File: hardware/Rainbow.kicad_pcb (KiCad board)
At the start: 2 copper layers, 53.2 x 38.7 mm, 22 parts, among them J1 PICKit3, J2 UART, J3 JUMPER, J4 JACK, J5 RGB, J6 RGB, J7 RGB, J8 RGB, J9 SOURCE, Q1 Q_NMOS_GDS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

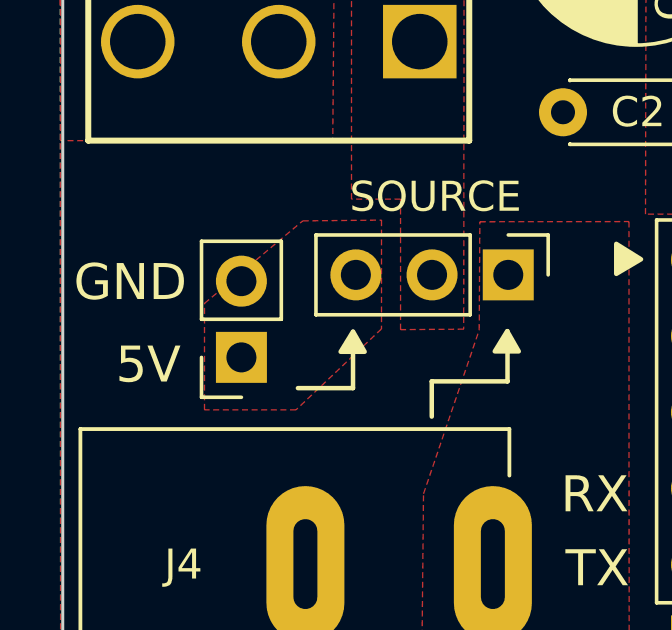
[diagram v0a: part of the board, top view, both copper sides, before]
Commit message: Folder renaming
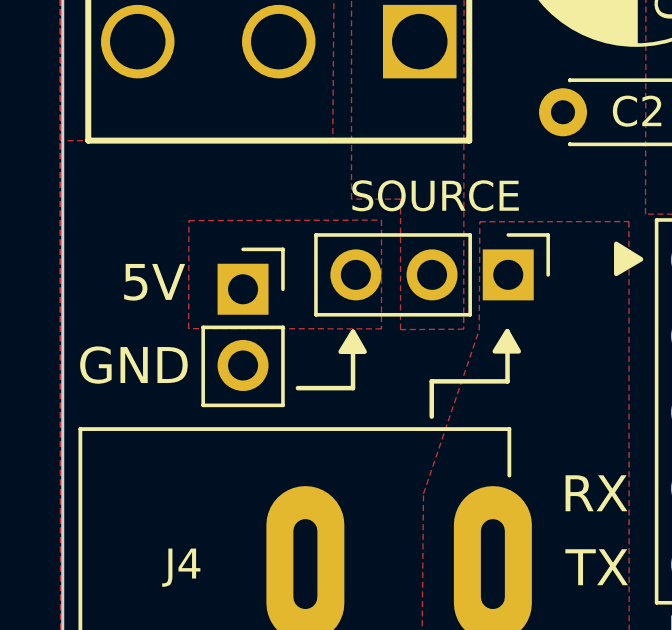
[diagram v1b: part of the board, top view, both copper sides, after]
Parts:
- moved J3 2.27 mm to (95.5, 77.4), turned to 0 degrees
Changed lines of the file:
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@@
   )
   (footprint "Connector_PinSocket_2.54mm:PinSocket_1x02_P2.54mm_Vertical" (layer "F.Cu")
-    (at 95.43 79.7 180)
+    (at 95.485 77.43)
     (descr "Through hole straight socket strip, 1x02, 2.54mm pitch, single row (from Kicad 4.0.7), script generated")
     (tags "Through hole socket strip THT 1x02 2.54mm single row")
@@
     (fp_line (start -1.27 -1.27) (end 0.635 -1.27) (layer "F.Fab") (width 0.1))
     (fp_line (start 0.635 -1.27) (end 1.27 -0.635) (layer "F.Fab") (width 0.1))
-    (pad "1" thru_hole rect (at 0 0 180) (size 1.7 1.7) (drill 1) (layers *.Cu *.Mask)
+    (pad "1" thru_hole rect (at 0 0) (size 1.7 1.7) (drill 1) (layers *.Cu *.Mask)
       (net 13 "Net-(J3-Pad1)") (pinfunction "Pin_1") (pintype "passive"))
-    (pad "2" thru_hole oval (at 0 2.54 180) (size 1.7 1.7) (drill 1) (layers *.Cu *.Mask)
+    (pad "2" thru_hole oval (at 0 2.54) (size 1.7 1.7) (drill 1) (layers *.Cu *.Mask)
       (net 1 "GNDREF") (pinfunction "Pin_2") (pintype "passive"))
     (model "${KICAD6_3DMODEL_DIR}/Connector_PinSocket_2.54mm.3dshapes/PinSocket_1x02_P2.54mm_Vertical.wrl"
@@
     (effects (font (size 1.2 1.2) (thickness 0.2)))
   )
-  (gr_text "GND" (at 91.725 77.2) (layer "F.SilkS")
+  (gr_text "GND" (at 91.85 80) (layer "F.SilkS")
     (effects (font (size 1.2 1.2) (thickness 0.2)))
   )
@@
     (effects (font (size 1.2 1.2) (thickness 0.2)))
   )
-  (gr_text "5V" (at 92.325 79.95) (layer "F.SilkS")
+  (gr_text "5V" (at 92.48 77.23) (layer "F.SilkS")
     (effects (font (size 1.2 1.2) (thickness 0.2)))
   )
@@
       (pts
         (xy 100.1 78.75)
-        (xy 97.25 81.45)
-        (xy 94.2 81.45)
-        (xy 94.2 77.9)
-        (xy 97.475 75.15)
+        (xy 93.67138 78.741393)
+        (xy 93.68138 75.141393)
         (xy 100.1 75.125)
       )

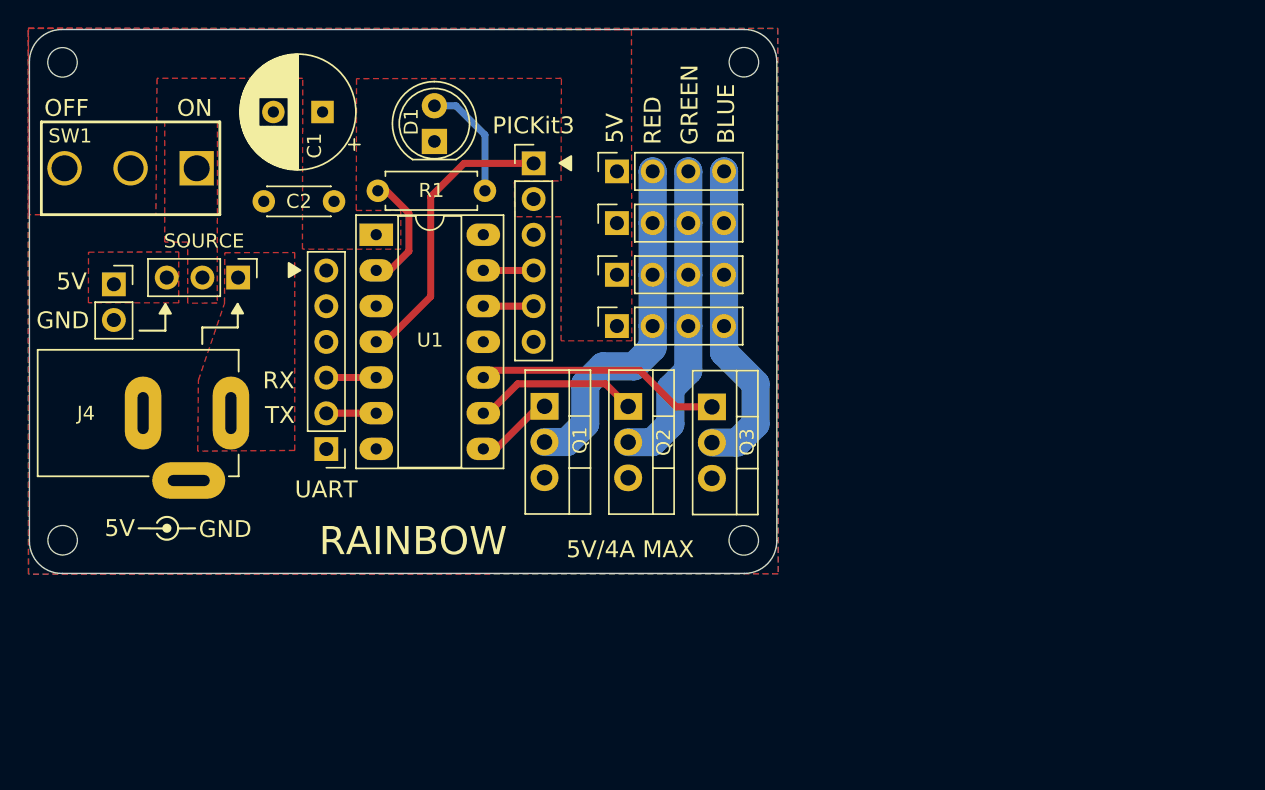
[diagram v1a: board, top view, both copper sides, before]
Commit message: Add fuse
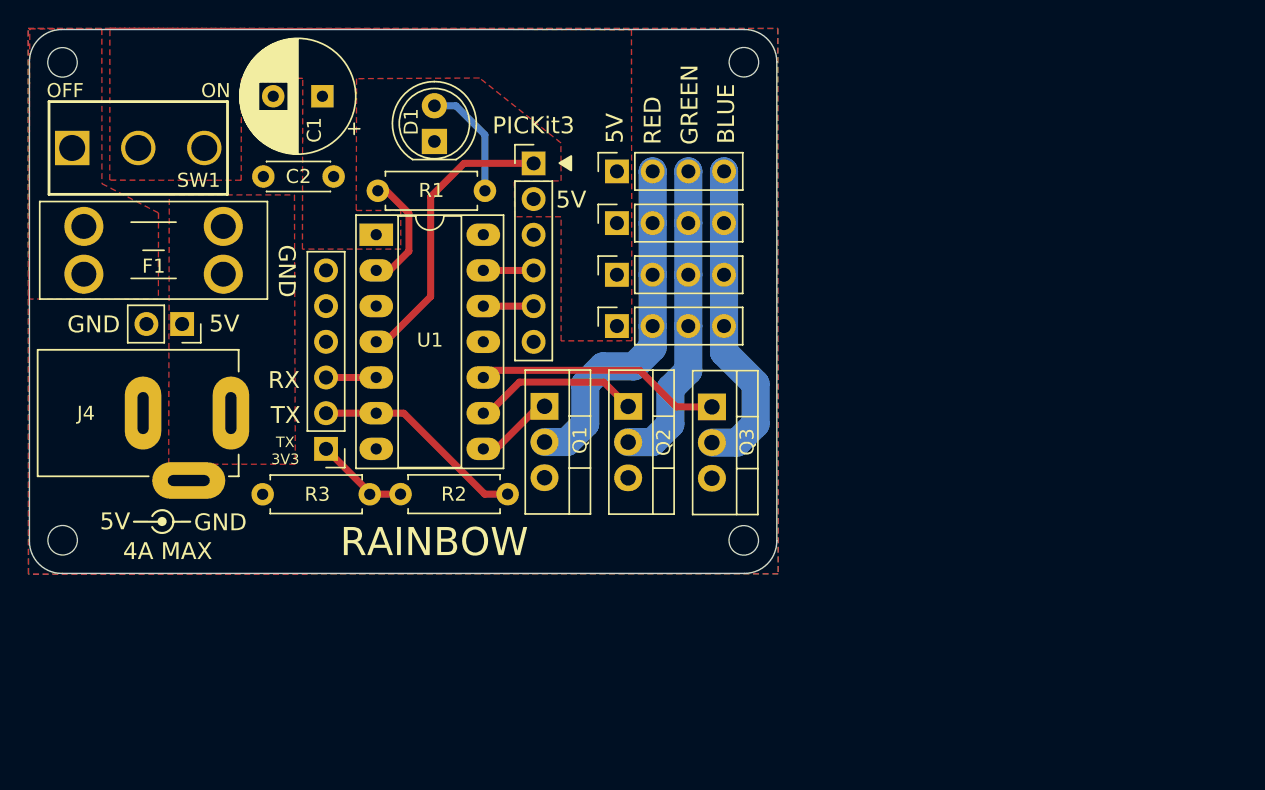
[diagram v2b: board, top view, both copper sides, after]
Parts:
- removed J9: SOURCE, Connector_PinHeader_2.54mm:PinHeader_1x03_P2.54mm_Vertical
- added F1: FUSE, Fuse:Fuseholder_Blade_Mini_Keystone_3568, F.Cu at (103.3, 76.7)
- added R2: 1K, Resistor_THT:R_Axial_DIN0207_L6.3mm_D2.5mm_P7.62mm_Horizontal, F.Cu at (123.5, 92.4)
- added R3: 2K, Resistor_THT:R_Axial_DIN0207_L6.3mm_D2.5mm_P7.62mm_Horizontal, F.Cu at (113.7, 92.4)
- moved J3 5.62 mm to (100.3, 80.3), turned to -90 degrees
- moved C2 1.77 mm to (111.1, 69.8)
- moved SW1 1.54 mm to (97.2, 67.7), turned to 90 degrees
- moved C1 1.12 mm to (110.3, 64.0)
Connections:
- J2 pad 1: unconnected-(J2-Pad1) -> Net-(J2-Pad1)
- J3 pad 1: Net-(J3-Pad1) -> Net-(J4-Pad1)
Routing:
- net TX: track 3.54 -> 15.3 mm
- net Net-(J2-Pad1): track 0.00 -> 6.58 mm
- removed copper zone on F.Cu, net Net-(J3-Pad1)
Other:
- board text added: "4A MAX"
- board text added: "TX 3V3"
- board text removed: "5V/4A MAX"
- board text removed: "SOURCE"
- board text removed: "UART"

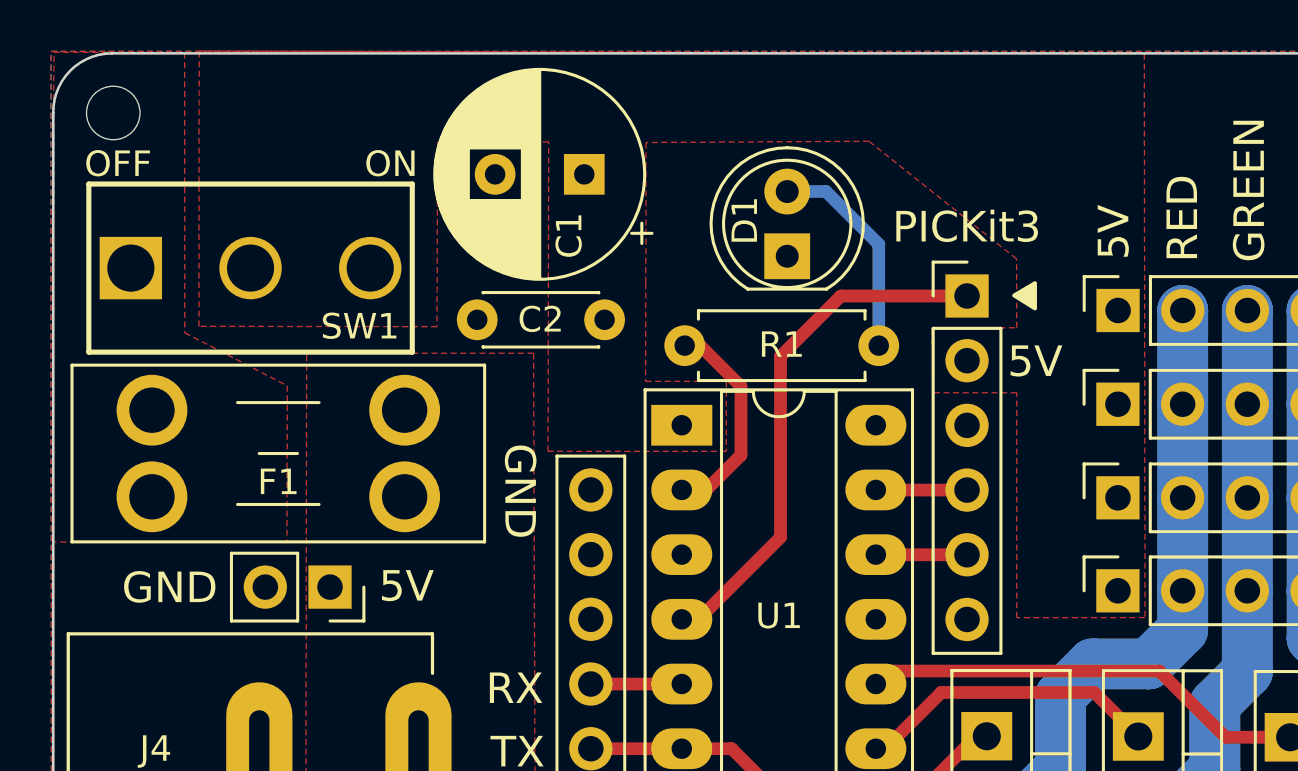
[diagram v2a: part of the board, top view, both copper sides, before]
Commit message: Bottom 5V polygons
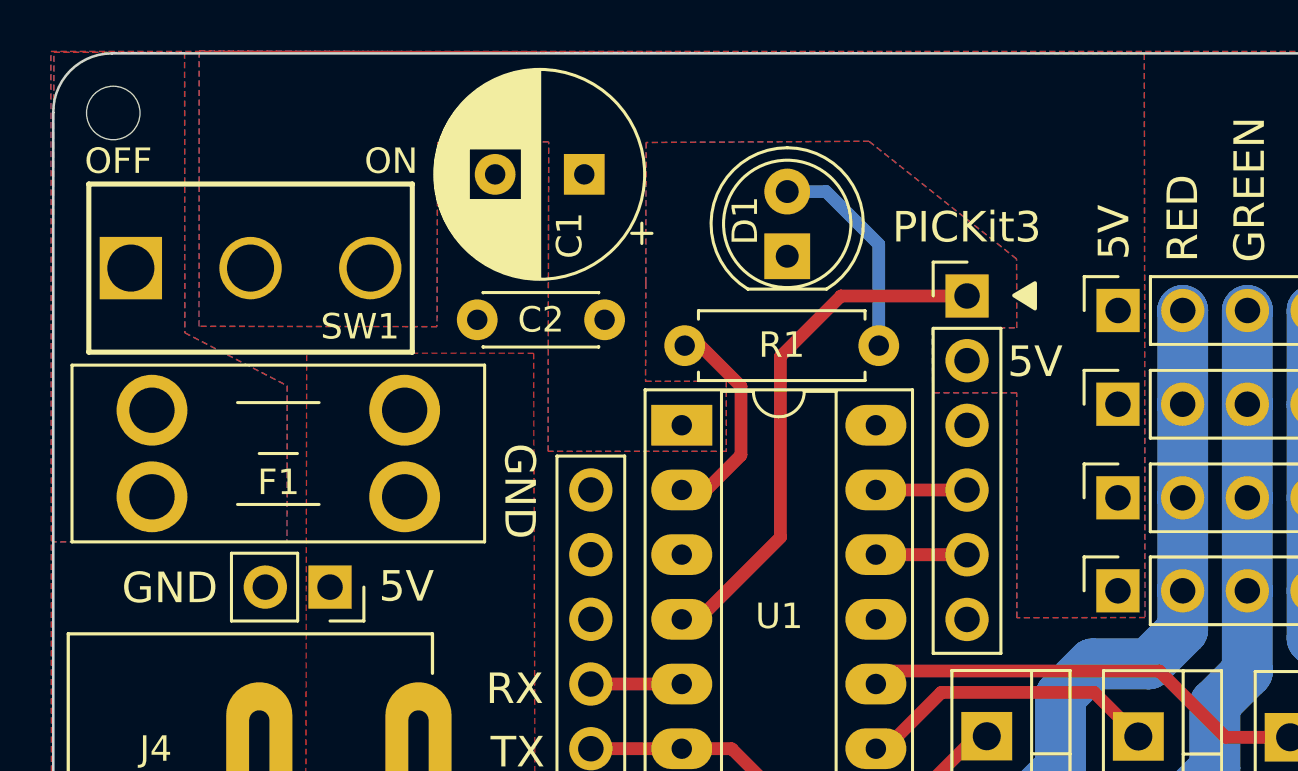
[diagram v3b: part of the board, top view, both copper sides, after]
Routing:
- added copper zone on B.Cu, net +5V
- added copper zone on B.Cu, net Net-(F1-Pad2)
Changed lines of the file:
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@@
     (effects (font (size 1.2 1.2) (thickness 0.2)))
   )
-  (gr_text "OFF" (at 92.02 63.65) (layer "F.SilkS")
+  (gr_text "OFF" (at 92.03 63.53) (layer "F.SilkS")
     (effects (font (size 1 1) (thickness 0.2)))
   )
-  (gr_text "ON" (at 102.74 63.65) (layer "F.SilkS")
+  (gr_text "ON" (at 102.74 63.53) (layer "F.SilkS")
     (effects (font (size 1 1) (thickness 0.2)))
   )
@@
   (segment (start 114.265 70.775) (end 114.875 70.775) (width 0.5) (layer "F.Cu") (net 19))
   (segment (start 115.11 76.44) (end 114.15 76.44) (width 0.5) (layer "F.Cu") (net 19))
-  (zone (net 4) (net_name "+5V") (layer "F.Cu") (hatch edge 0.508)
+  (zone (net 4) (net_name "+5V") (layers F&B.Cu) (hatch edge 0.508)
     (priority 1)
     (connect_pads (clearance 0.508))
@@
     )
   )
-  (zone (net 23) (net_name "Net-(F1-Pad2)") (layer "F.Cu") (hatch edge 0.508)
+  (zone (net 23) (net_name "Net-(F1-Pad2)") (layers F&B.Cu) (hatch edge 0.508)
     (priority 1)
     (connect_pads (clearance 0.508))
@@
     (connect_pads (clearance 0.508))
     (min_thickness 0.254) (filled_areas_thickness no)
-    (fill yes (thermal_gap 0.508) (thermal_bridge_width 0.508) (smoothing fillet) (radius 1))
+    (fill yes (thermal_gap 0.508) (thermal_bridge_width 0.508) (smoothing fillet) (radius 1) (island_removal_mode 2) (island_area_min 10))
     (polygon
       (pts

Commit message: Finish up PCB
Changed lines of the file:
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@@
   (net 22 "unconnected-(U1-Pad11)")
   (net 23 "Net-(F1-Pad2)")
-  (net 24 "Net-(J4-Pad1)")
+  (net 24 "Net-(F1-Pad1)")
   (footprint "Connector_PinSocket_2.54mm:PinSocket_1x04_P2.54mm_Vertical" (layer "F.Cu")
     (at 131.275 73.075 90)
@@
     (fp_line (start 12.96 -1.67) (end -3.04 -1.67) (layer "F.Fab") (width 0.1))
     (pad "1" thru_hole circle (at 0 3.4 180) (size 2.78 2.78) (drill 1.78) (layers *.Cu *.Mask)
-      (net 24 "Net-(J4-Pad1)") (pintype "passive"))
+      (net 24 "Net-(F1-Pad1)") (pintype "passive"))
     (pad "1" thru_hole circle (at 0 0 180) (size 2.78 2.78) (drill 1.78) (layers *.Cu *.Mask)
-      (net 24 "Net-(J4-Pad1)") (pintype "passive"))
+      (net 24 "Net-(F1-Pad1)") (pintype "passive"))
     (pad "2" thru_hole circle (at 9.92 0 180) (size 2.78 2.78) (drill 1.78) (layers *.Cu *.Mask)
       (net 23 "Net-(F1-Pad2)") (pintype "passive"))
@@
     (fp_line (start 0 -4.5) (end 14.3 -4.5) (layer "F.Fab") (width 0.127))
     (pad "1" thru_hole oval (at 13.75 0) (size 2.6 5.2) (drill oval 0.8 3) (layers *.Cu *.Mask)
-      (net 24 "Net-(J4-Pad1)") (pintype "passive"))
+      (net 24 "Net-(F1-Pad1)") (pintype "passive"))
     (pad "2" thru_hole oval (at 7.5 0) (size 2.6 5.2) (drill oval 0.8 3) (layers *.Cu *.Mask)
       (net 1 "GNDREF") (pintype "passive"))
@@
     (fp_line (start 0.635 -1.27) (end 1.27 -0.635) (layer "F.Fab") (width 0.1))
     (pad "1" thru_hole rect (at 0 0 270) (size 1.7 1.7) (drill 1) (layers *.Cu *.Mask)
-      (net 24 "Net-(J4-Pad1)") (pinfunction "Pin_1") (pintype "passive"))
+      (net 24 "Net-(F1-Pad1)") (pinfunction "Pin_1") (pintype "passive"))
     (pad "2" thru_hole oval (at 0 2.54 270) (size 1.7 1.7) (drill 1) (layers *.Cu *.Mask)
       (net 1 "GNDREF") (pinfunction "Pin_2") (pintype "passive"))
@@
     (effects (font (size 1.2 1.2) (thickness 0.2)))
   )
-  (gr_text "RAINBOW" (at 118.28 95.77) (layer "F.SilkS")
+  (gr_text "RAINBOW" (at 117.83 95.74) (layer "F.SilkS")
     (effects (font (size 2 2) (thickness 0.4)))
   )
@@
     (effects (font (size 1.2 1.2) (thickness 0.2)))
   )
-  (gr_text "OFF" (at 92.03 63.53) (layer "F.SilkS")
+  (gr_text "OFF" (at 92.11 63.5 180) (layer "F.SilkS")
     (effects (font (size 1 1) (thickness 0.2)))
   )
-  (gr_text "ON" (at 102.74 63.53) (layer "F.SilkS")
+  (gr_text "ON" (at 102.75 63.5 180) (layer "F.SilkS")
     (effects (font (size 1 1) (thickness 0.2)))
   )
@@
     )
   )
-  (zone (net 24) (net_name "Net-(J4-Pad1)") (layer "F.Cu") (hatch edge 0.508)
+  (zone (net 24) (net_name "Net-(F1-Pad1)") (layer "F.Cu") (hatch edge 0.508)
     (priority 1)
     (connect_pads (clearance 0.508))

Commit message: Notes for hardware rework
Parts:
- added D2: LED, LED_THT:LED_D5.0mm, F.Cu at (97.6, 64.4)
- added R4: 270R, Resistor_THT:R_Axial_DIN0207_L6.3mm_D2.5mm_P7.62mm_Horizontal, F.Cu at (102.3, 63.5)
- moved C1 5.44 mm to (110.3, 69.5)
- moved C2 4.69 mm to (115.4, 67.9), turned to 90 degrees
- moved F1 2.05 mm to (103.2, 78.8)
- moved J3 2.05 mm to (100.3, 82.3)
- moved J4 2.05 mm to (90.0, 88.6)
- moved SW1 2.05 mm to (97.2, 69.8)
- moved D1 1.88 mm to (120.2, 67.3)
